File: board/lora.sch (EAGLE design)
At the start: 29 parts, among them J1 SWD_PTH_SHROUD, X1 SMA-142-0701-801/806

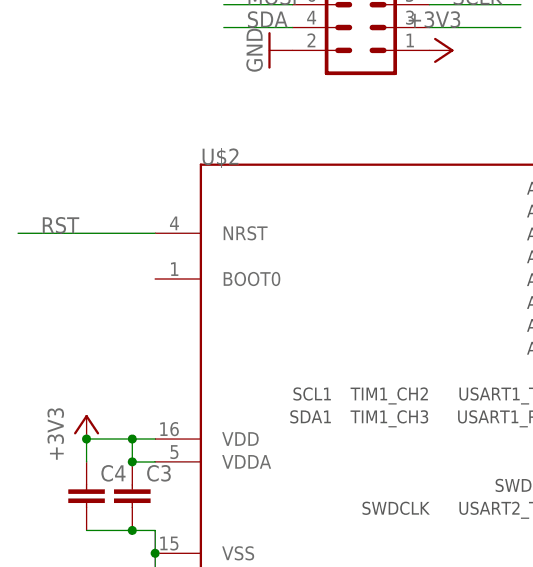
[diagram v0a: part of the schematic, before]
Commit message: added boot0 to tracker, some wiring on basestation
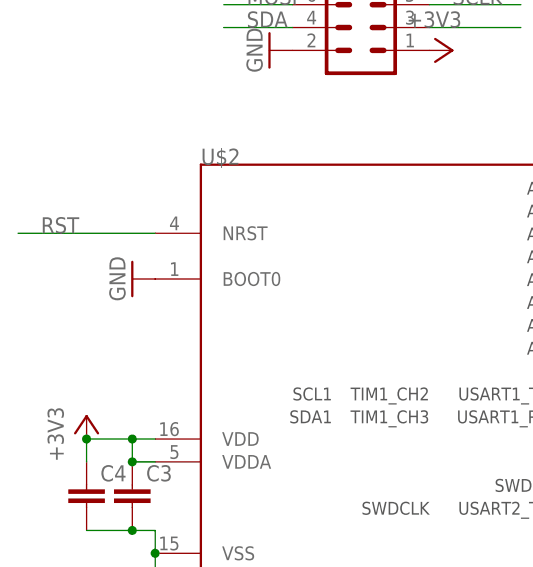
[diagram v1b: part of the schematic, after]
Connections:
- net GND: now also U$2.BOOT0
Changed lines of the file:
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@@
 <part name="TP2" library="testpad" deviceset="PTR1" device="B1,27"/>
 <part name="GND20" library="supply1" deviceset="GND" device=""/>
+<part name="GND21" library="supply1" deviceset="GND" device=""/>
 </parts>
 <sheets>
@@
 <instance part="TP2" gate="G$1" x="241.3" y="-43.18" rot="R90"/>
 <instance part="GND20" gate="1" x="236.22" y="-43.18" rot="MR90"/>
+<instance part="GND21" gate="1" x="12.7" y="20.32" rot="R270"/>
 </instances>
 <busses>
@@
 <pinref part="GND20" gate="1" pin="GND"/>
 </segment>
+<segment>
+<pinref part="U$2" gate="G$1" pin="BOOT0"/>
+<pinref part="GND21" gate="1" pin="GND"/>
+</segment>
 </net>

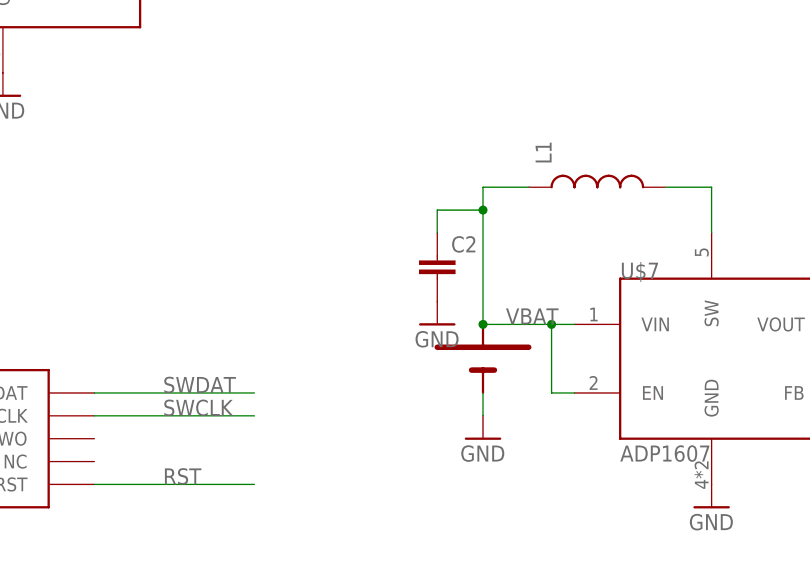
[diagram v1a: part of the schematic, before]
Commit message: initial route
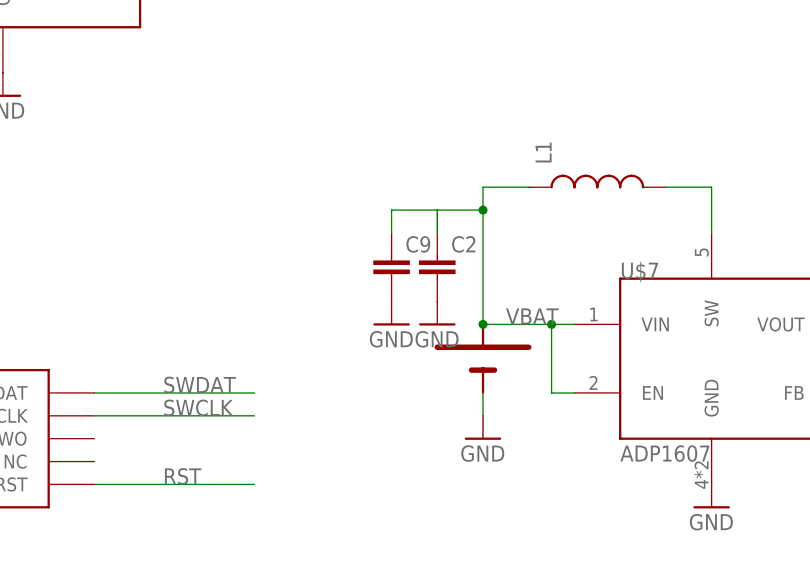
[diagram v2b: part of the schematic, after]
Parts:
- added C9: (no value), rcl:C-EUC0603
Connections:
- net GND: now also C9.2
- net VBAT: now also C9.1
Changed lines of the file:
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@@
 <part name="GND20" library="supply1" deviceset="GND" device=""/>
 <part name="GND21" library="supply1" deviceset="GND" device=""/>
+<part name="C9" library="rcl" deviceset="C-EU" device="C0603"/>
+<part name="GND22" library="supply1" deviceset="GND" device=""/>
 </parts>
 <sheets>
@@
 <instance part="GND20" gate="1" x="236.22" y="-43.18" rot="MR90"/>
 <instance part="GND21" gate="1" x="12.7" y="20.32" rot="R270"/>
+<instance part="C9" gate="G$1" x="127" y="76.2"/>
+<instance part="GND22" gate="1" x="127" y="68.58"/>
 </instances>
 <busses>
@@
 <pinref part="U$2" gate="G$1" pin="BOOT0"/>
 <pinref part="GND21" gate="1" pin="GND"/>
+</segment>
+<segment>
+<pinref part="C9" gate="G$1" pin="2"/>
+<pinref part="GND22" gate="1" pin="GND"/>
 </segment>
 </net>
@@
 <junction x="137.16" y="81.28"/>
 <label x="139.7" y="68.58" size="1.778" layer="95"/>
-</segment>
-</net>
+<pinref part="C9" gate="G$1" pin="1"/>
+<wire x1="132.08" y1="81.28" x2="127" y2="81.28" width="0.1524" layer="91"/>
+<wire x1="127" y1="81.28" x2="127" y2="78.74" width="0.1524" layer="91"/>
+</segment>
+</net>

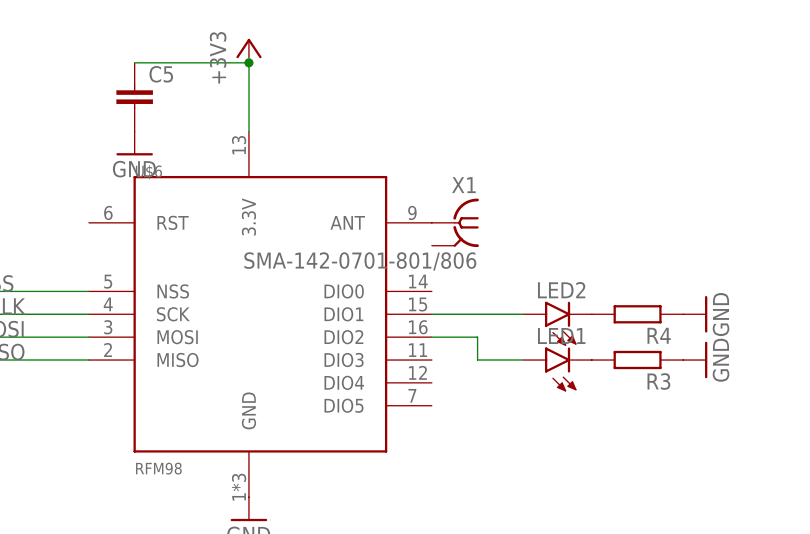
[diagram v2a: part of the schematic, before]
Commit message: adding interrupt line to raido
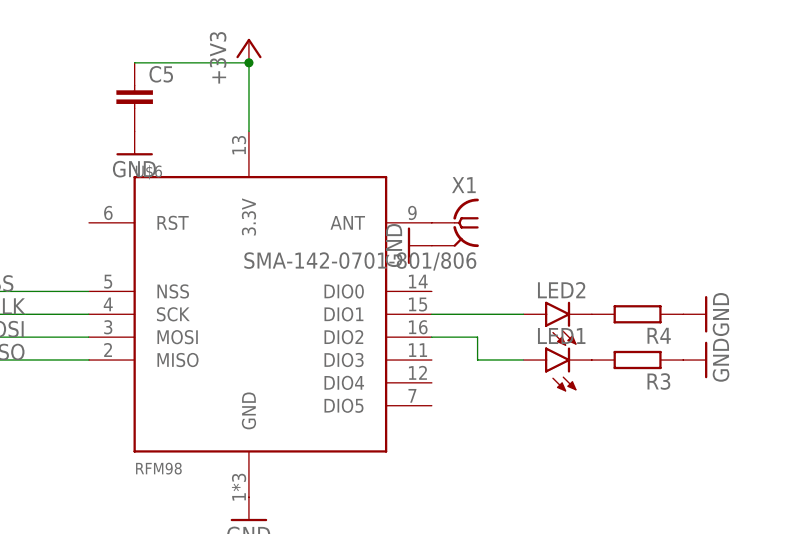
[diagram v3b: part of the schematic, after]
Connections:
- net GND: now also X1.2
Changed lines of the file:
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@@
 <part name="C9" library="rcl" deviceset="C-EU" device="C0603"/>
 <part name="GND22" library="supply1" deviceset="GND" device=""/>
+<part name="GND23" library="supply1" deviceset="GND" device=""/>
 </parts>
 <sheets>
@@
 <instance part="C9" gate="G$1" x="127" y="76.2"/>
 <instance part="GND22" gate="1" x="127" y="68.58"/>
+<instance part="GND23" gate="1" x="101.6" y="124.46" rot="R270"/>
 </instances>
 <busses>
@@
 <pinref part="GND22" gate="1" pin="GND"/>
 </segment>
+<segment>
+<pinref part="X1" gate="G1" pin="2"/>
+<pinref part="GND23" gate="1" pin="GND"/>
+</segment>
 </net>

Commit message: some stuff changed lol
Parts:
- added L3: (no value), SparkFun-Passives:INDUCTOR1210
- added S1: SWITCH-MOMENTARY-2SMD, Mine:SWITCH-MOMENTARY-2SMD
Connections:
- removed net N$12: LED1.A, U$6.DIO2
- net +3V3: now also LED2.A
- net GND: now also LED1.C, S1.1; no longer R3.1, R4.1
- net N$3: now also L3.2
- net N$5: now also LED1.A, R3.1, S1.2; no longer LED1.C, R3.2
- net N$8: now also R3.2, R4.1, U$2.PB1; no longer LED2.A, U$6.DIO1
- net VBAT: now also L3.1
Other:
- moved on the sheet: LED1, LED2, R3, R4
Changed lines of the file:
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@@
 <part name="R3" library="rcl" deviceset="R-EU_" device="R0603"/>
 <part name="R4" library="rcl" deviceset="R-EU_" device="R0603"/>
-<part name="GND17" library="supply1" deviceset="GND" device=""/>
-<part name="GND18" library="supply1" deviceset="GND" device=""/>
 <part name="R5" library="rcl" deviceset="R-EU_" device="R0603"/>
 <part name="+3V8" library="supply1" deviceset="+3V3" device=""/>
@@
 <part name="GND22" library="supply1" deviceset="GND" device=""/>
 <part name="GND23" library="supply1" deviceset="GND" device=""/>
+<part name="GND17" library="supply1" deviceset="GND" device=""/>
+<part name="+3V3" library="supply1" deviceset="+3V3" device=""/>
+<part name="S1" library="Mine" deviceset="SWITCH-MOMENTARY-2" device="SMD"/>
+<part name="L3" library="SparkFun-Passives" deviceset="INDUCTOR" device="1210"/>
 </parts>
 <sheets>
@@
 <instance part="GND16" gate="1" x="27.94" y="45.72" rot="R270"/>
 <instance part="+3V7" gate="G$1" x="48.26" y="45.72" rot="R270"/>
-<instance part="LED1" gate="G$1" x="116.84" y="111.76" rot="R90"/>
-<instance part="LED2" gate="G$1" x="116.84" y="116.84" rot="R90"/>
-<instance part="R3" gate="G$1" x="127" y="111.76" rot="R180"/>
-<instance part="R4" gate="G$1" x="127" y="116.84" rot="R180"/>
-<instance part="GND17" gate="1" x="134.62" y="116.84" rot="R90"/>
-<instance part="GND18" gate="1" x="134.62" y="111.76" rot="R90"/>
+<instance part="LED1" gate="G$1" x="109.22" y="-33.02"/>
+<instance part="LED2" gate="G$1" x="109.22" y="-5.08"/>
+<instance part="R3" gate="G$1" x="109.22" y="-25.4" rot="R90"/>
+<instance part="R4" gate="G$1" x="109.22" y="-15.24" rot="R90"/>
 <instance part="R5" gate="G$1" x="96.52" y="27.94" rot="R180"/>
 <instance part="+3V8" gate="G$1" x="7.62" y="5.08"/>
@@
 <instance part="GND22" gate="1" x="127" y="68.58"/>
 <instance part="GND23" gate="1" x="101.6" y="124.46" rot="R270"/>
+<instance part="GND17" gate="1" x="109.22" y="-43.18"/>
+<instance part="+3V3" gate="G$1" x="109.22" y="0"/>
+<instance part="S1" gate="G$1" x="101.6" y="-35.56" rot="R90"/>
+<instance part="L3" gate="G$1" x="149.86" y="88.9" rot="R90"/>
 </instances>
 <busses>
@@
 <wire x1="157.48" y1="83.82" x2="162.56" y2="83.82" width="0.1524" layer="91"/>
 <wire x1="162.56" y1="83.82" x2="162.56" y2="78.74" width="0.1524" layer="91"/>
+<pinref part="L3" gate="G$1" pin="2"/>
+<wire x1="157.48" y1="88.9" x2="157.48" y2="83.82" width="0.1524" layer="91"/>
 </segment>
 </net>
@@
 </segment>
 <segment>
-<pinref part="R4" gate="G$1" pin="1"/>
-<pinref part="GND17" gate="1" pin="GND"/>
-</segment>
-<segment>
-<pinref part="R3" gate="G$1" pin="1"/>
-<pinref part="GND18" gate="1" pin="GND"/>
-</segment>
-<segment>
 <pinref part="L2" gate="G$1" pin="2"/>
 <pinref part="GND19" gate="1" pin="GND"/>
@@
 <pinref part="X1" gate="G1" pin="2"/>
 <pinref part="GND23" gate="1" pin="GND"/>
+</segment>
+<segment>
+<pinref part="GND17" gate="1" pin="GND"/>
+<pinref part="LED1" gate="G$1" pin="C"/>
+<pinref part="S1" gate="G$1" pin="1"/>
+<wire x1="109.22" y1="-40.64" x2="101.6" y2="-40.64" width="0.1524" layer="91"/>
+<junction x="109.22" y="-40.64"/>
+<wire x1="109.22" y1="-40.64" x2="109.22" y2="-38.1" width="0.1524" layer="91"/>
 </segment>
 </net>
@@
 <junction x="7.62" y="2.54"/>
 </segment>
+<segment>
+<pinref part="LED2" gate="G$1" pin="A"/>
+<pinref part="+3V3" gate="G$1" pin="+3V3"/>
+</segment>
 </net>
 <net name="SWDAT" class="0">
@@
 </segment>
 </net>
-<net name="N$5" class="0">
-<segment>
-<pinref part="LED1" gate="G$1" pin="C"/>
-<pinref part="R3" gate="G$1" pin="2"/>
-</segment>
-</net>
 <net name="N$7" class="0">
 <segment>
 <pinref part="LED2" gate="G$1" pin="C"/>
 <pinref part="R4" gate="G$1" pin="2"/>
-</segment>
-</net>
-<net name="N$8" class="0">
-<segment>
-<pinref part="U$6" gate="G$1" pin="DIO1"/>
-<pinref part="LED2" gate="G$1" pin="A"/>
-<wire x1="104.14" y1="116.84" x2="114.3" y2="116.84" width="0.1524" layer="91"/>
-</segment>
-</net>
-<net name="N$12" class="0">
-<segment>
-<pinref part="U$6" gate="G$1" pin="DIO2"/>
-<wire x1="104.14" y1="114.3" x2="109.22" y2="114.3" width="0.1524" layer="91"/>
-<wire x1="109.22" y1="114.3" x2="109.22" y2="111.76" width="0.1524" layer="91"/>
-<pinref part="LED1" gate="G$1" pin="A"/>
-<wire x1="109.22" y1="111.76" x2="114.3" y2="111.76" width="0.1524" layer="91"/>
 </segment>
 </net>
@@
 <wire x1="132.08" y1="81.28" x2="127" y2="81.28" width="0.1524" layer="91"/>
 <wire x1="127" y1="81.28" x2="127" y2="78.74" width="0.1524" layer="91"/>
+<pinref part="L3" gate="G$1" pin="1"/>
+<wire x1="142.24" y1="88.9" x2="142.24" y2="83.82" width="0.1524" layer="91"/>
 </segment>
 </net>
@@
 </segment>
 </net>
+<net name="N$8" class="0">
+<segment>
+<pinref part="U$2" gate="G$1" pin="PB1"/>
+<wire x1="73.66" y1="-12.7" x2="93.98" y2="-12.7" width="0.1524" layer="91"/>
+<wire x1="93.98" y1="-20.32" x2="93.98" y2="-12.7" width="0.1524" layer="91"/>
+<pinref part="R3" gate="G$1" pin="2"/>
+<wire x1="109.22" y1="-20.32" x2="93.98" y2="-20.32" width="0.1524" layer="91"/>
+<pinref part="R4" gate="G$1" pin="1"/>
+<junction x="109.22" y="-20.32"/>
+</segment>
+</net>
+<net name="N$5" class="0">
+<segment>
+<pinref part="R3" gate="G$1" pin="1"/>
+<pinref part="LED1" gate="G$1" pin="A"/>
+<pinref part="S1" gate="G$1" pin="2"/>
+<wire x1="109.22" y1="-30.48" x2="101.6" y2="-30.48" width="0.1524" layer="91"/>
+<junction x="109.22" y="-30.48"/>
+</segment>
+</net>

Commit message: adding stuff to silk
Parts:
- removed SV1: (no value), con-ml:ML10
- removed U$1: KEYSTONE-53, Mine:KEYSTONE-53
- added JP1: M05X2SHD, SparkFun-Connectors:M05X2SHD
- added X3: RFM98, Mine:RFM98
- C1: value (none) -> 4u7; device rcl:C-EUC0805 -> rcl:C-EUC0603
- C2: value (none) -> 100n; device rcl:C-EUC0805 -> rcl:C-EUC0603
- C3, C6: value (none) -> 10u; device rcl:C-EUC0603 -> rcl:C-EUC0805
- C4, C5, C7: value (none) -> 1u
- C8: value (none) -> 100n
- L1: value (none) -> 2u2
- R1, R2: value (none) -> 330
- R3: value (none) -> 360k
- R4: value (none) -> 220k
- R5: value (none) -> 10k
- U$6: value RFM98 -> KEYSTONE-53; device Mine:RFM98 -> Mine:KEYSTONE-53
- renumbered U$2 to IC1, U$3 to X2, U$4 to U$5, U$7 to IC2
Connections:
- net +3V3: now also C2.1, C8.1, JP1.1, LED1.A, R3.2, X3.3.3V; no longer C4.1, C6.1, LED2.A, R1.2, SV1.1, U$6.3.3V
- net GND: now also C8.2, JP1.2, LED2.C, R4.1, TP1.TP, U$6.-, X3.GND; no longer C9.2, LED1.C, R2.1, SV1.2, TP2.TP, U$1.-, U$6.GND
- net GPIO1: now also JP1.8; no longer SV1.8
- net GPIO2: now also JP1.9; no longer SV1.9
- net GPIO3: now also JP1.10; no longer SV1.10
- net MISO: now also JP1.7, X3.MISO; no longer SV1.7, U$6.MISO
- net MOSI: now also JP1.6, X3.MOSI; no longer SV1.6, U$6.MOSI
- net N$1: now also C9.2; no longer C8.2
- net N$2: now also X3.ANT; no longer U$6.ANT
- net N$4: now also C9.1; no longer C8.1
- net N$5: now also LED2.A, R2.1; no longer LED1.A, R3.1
- net N$6: now also R3.1, R4.2; no longer R1.1, R2.2
- net N$7: now also LED1.C, R1.2; no longer LED2.C, R4.2
- net N$8: now also R1.1, R2.2; no longer R3.2, R4.1
- net NSS: now also X3.NSS; no longer U$6.NSS
- net SCL: now also JP1.3; no longer SV1.3
- net SCLK: now also JP1.5, X3.SCK; no longer SV1.5, U$6.SCK
- net SDA: now also JP1.4; no longer SV1.4
- net UART_RX: now also TP2.TP; no longer TP3.TP
- net UART_TX: now also TP3.TP; no longer TP1.TP
- net VBAT: now also C4.1, C6.1, U$6.+; no longer C2.1, C9.1, U$1.+
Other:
- moved on the sheet: C1, C2, C3, C4, C5, C6, C7, C8, C9, LED1, LED2, R1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

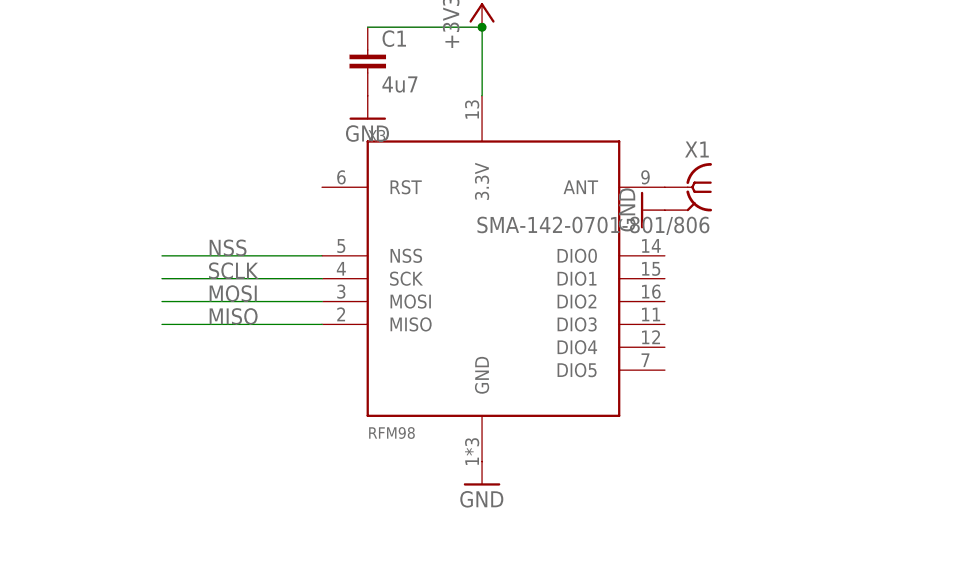
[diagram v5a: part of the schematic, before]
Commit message: connecting clkout
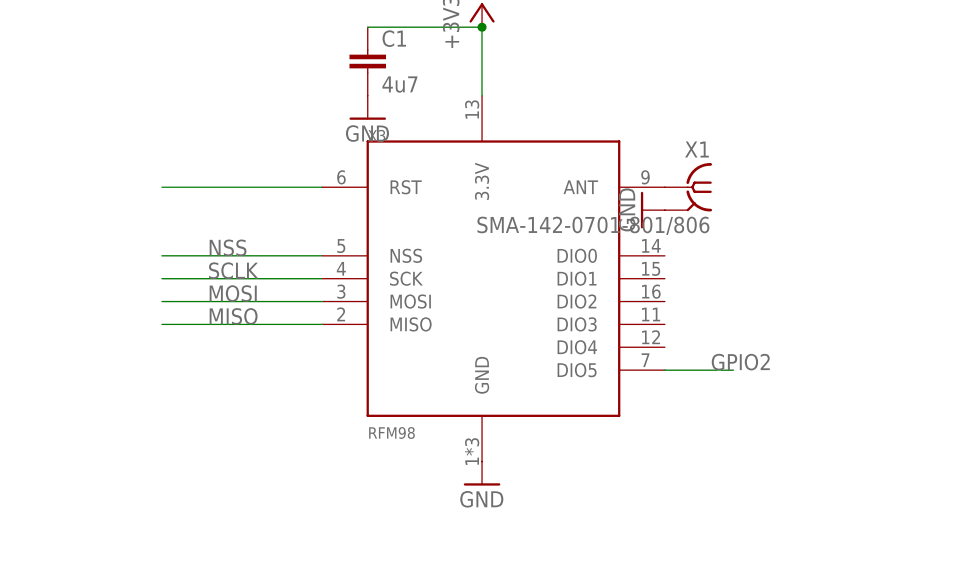
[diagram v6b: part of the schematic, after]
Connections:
- new net N$10: X3.RST
- net GPIO2: now also X3.DIO5
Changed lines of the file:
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@@
 <pinref part="IC1" gate="G$1" pin="PF0"/>
+</segment>
+<segment>
+<pinref part="X3" gate="G$1" pin="DIO5"/>
+<wire x1="104.14" y1="106.68" x2="111.76" y2="106.68" width="0.1524" layer="91"/>
+<label x="109.22" y="106.68" size="1.778" layer="95"/>
 </segment>
 </net>
@@
 </segment>
 </net>
+<net name="N$10" class="0">
+<segment>
+<pinref part="X3" gate="G$1" pin="RST"/>
+<wire x1="66.04" y1="127" x2="48.26" y2="127" width="0.1524" layer="91"/>
+</segment>
+</net>
